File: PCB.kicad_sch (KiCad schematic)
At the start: 57 parts, among them J1 USB_C_Receptacle_USB2.0_16P, J10 Conn_01x05_Pin, J11 Conn_01x05_Pin, J12 Conn_01x03_Pin, J2 Conn_01x04_Pin, J3 Conn_01x04_Pin, J4 Conn_01x07_Pin, J5 Conn_01x02_Pin, J6 Conn_01x02_Pin, J7 Conn_01x02_Pin, J8 Conn_01x04_Pin, J9 Conn_01x07_Pin, SW1 SW_Push, SW2 SW_Push, U1 TMC2209_SILENTSTEPSTICK, U2 TMC2209_SILENTSTEPSTICK, U3 D3V3XA4B10LP, U4 AMS1117-3.3 (UMW), U5 TMC2209_SILENTSTEPSTICK, U6 ESP32-S3-WROOM-1

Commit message: Dernier DRC après modicifications
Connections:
- net GND: now also J11.1 (Pin_1), J11.2 (Pin_2), J11.3 (Pin_3), J11.4 (Pin_4)
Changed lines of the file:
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@@
 	)
 	(junction
+		(at 393.7 130.81)
+		(diameter 0)
+		(color 0 0 0 0)
+	)
+	(junction
 		(at 373.38 146.05)
 		(diameter 0)
@@
 	)
 	(junction
+		(at 386.08 130.81)
+		(diameter 0)
+		(color 0 0 0 0)
+	)
+	(junction
 		(at 290.83 176.53)
 		(diameter 0)
@@
 	)
 	(junction
+		(at 388.62 130.81)
+		(diameter 0)
+		(color 0 0 0 0)
+	)
+	(junction
 		(at 64.77 149.86)
 		(diameter 0)
@@
 	)
 	(junction
+		(at 391.16 130.81)
+		(diameter 0)
+		(color 0 0 0 0)
+	)
+	(junction
 		(at 373.38 143.51)
 		(diameter 0)
@@
 	(wire
 		(pts
+			(xy 388.62 130.81) (xy 391.16 130.81)
+		)
+		(stroke
+			(width 0)
+			(type default)
+		)
+	)
+	(wire
+		(pts
 			(xy 71.12 222.25) (xy 80.01 222.25)
 		)
@@
 	(wire
 		(pts
+			(xy 386.08 130.81) (xy 388.62 130.81)
+		)
+		(stroke
+			(width 0)
+			(type default)
+		)
+	)
+	(wire
+		(pts
 			(xy 71.12 222.25) (xy 71.12 223.52)
 		)
@@
 	(wire
 		(pts
+			(xy 393.7 130.81) (xy 396.24 130.81)
+		)
+		(stroke
+			(width 0)
+			(type default)
+		)
+	)
+	(wire
+		(pts
 			(xy 181.61 233.68) (xy 189.23 233.68)
 		)
@@
 	(wire
 		(pts
+			(xy 391.16 130.81) (xy 393.7 130.81)
+		)
+		(stroke
+			(width 0)
+			(type default)
+		)
+	)
+	(wire
+		(pts
 			(xy 74.93 58.42) (xy 80.01 58.42)
 		)
@@
 	(wire
 		(pts
-			(xy 396.24 130.81) (xy 396.24 140.97)
-		)
-		(stroke
-			(width 0)
-			(type default)
-		)
-	)
-	(wire
-		(pts
 			(xy 34.29 124.46) (xy 39.37 124.46)
 		)
@@
 	(symbol
 		(lib_id "power:GND")
-		(at 396.24 140.97 0)
+		(at 386.08 130.81 270)
 		(unit 1)
 		(exclude_from_sim no)
@@
 		(fields_autoplaced yes)
 		(property "Reference" "#PWR033"
-			(at 396.24 147.32 0)
+			(at 379.73 130.81 0)
 			(effects
 				(font
@@
 		)
 		(property "Value" "GND"
-			(at 396.24 146.05 0)
+			(at 382.27 130.8099 90)
 			(effects
 				(font
 					(size 1.27 1.27)
 				)
+				(justify right)
 			)
 		)
 		(property "Footprint" ""
-			(at 396.24 140.97 0)
+			(at 386.08 130.81 0)
 			(effects
 				(font
@@
 		)
 		(property "Datasheet" ""
-			(at 396.24 140.97 0)
+			(at 386.08 130.81 0)
 			(effects
 				(font
@@
 		)
 		(property "Description" "Power symbol creates a global label with name \"GND\" , ground"
-			(at 396.24 140.97 0)
+			(at 386.08 130.81 0)
 			(effects
 				(font

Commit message: Test DRC OK
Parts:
- C5: footprint Resistor_SMD:R_0603_1608Metric -> Capacitor_SMD:C_1206_3216Metric_Pad1.33x1.80mm_HandSolder
- R2, R3: footprint Resistor_SMD:R_01005_0402Metric -> Resistor_SMD:R_0805_2012Metric_Pad1.20x1.40mm_HandSolder
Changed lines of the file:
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@@
 			)
 		)
-		(property "Footprint" "Resistor_SMD:R_01005_0402Metric"
+		(property "Footprint" "Resistor_SMD:R_0805_2012Metric_Pad1.20x1.40mm_HandSolder"
 			(at 78.232 50.8 90)
 			(effects
@@
 			)
 		)
-		(property "Footprint" "Resistor_SMD:R_0603_1608Metric"
+		(property "Footprint" "Capacitor_SMD:C_1206_3216Metric_Pad1.33x1.80mm_HandSolder"
 			(at 122.8852 134.62 0)
 			(effects
@@
 			)
 		)
-		(property "Footprint" "Resistor_SMD:R_01005_0402Metric"
+		(property "Footprint" "Resistor_SMD:R_0805_2012Metric_Pad1.20x1.40mm_HandSolder"
 			(at 73.152 54.61 90)
 			(effects

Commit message: V2 avec test DRC OK
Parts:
- removed ADD1, J2, UART1: Conn_01x04_Pin, Connector_PinHeader_2.54mm:PinHeader_1x04_P2.54mm_Vertical, symbol Connector:Conn_01x04_Pin
- removed C6: 100uF, Capacitor_THT:CP_Radial_D10.0mm_P5.00mm, symbol Device:C
- removed J4: Conn_01x07_Pin, Connector_PinHeader_2.54mm:PinHeader_1x04_P2.54mm_Vertical, symbol Connector:Conn_01x04_Pin
- removed J9: Conn_01x07_Pin, Connector_PinHeader_2.54mm:PinHeader_1x03_P2.54mm_Vertical, symbol Connector:Conn_01x03_Pin
- removed JP3, JP4: Jumper_2_Open, Connector_PinHeader_2.54mm:PinHeader_1x02_P2.54mm_Vertical, symbol Jumper:Jumper_2_Open
- removed TOF1, TOF2, TOF3: Conn_01x05_Pin, Connector_PinHeader_2.54mm:PinHeader_1x05_P2.54mm_Vertical, symbol Connector:Conn_01x05_Pin
- removed U2: TMC2209_SILENTSTEPSTICK, TMC2209:MODULE_TMC2209_SILENTSTEPSTICK, symbol TMC2209_SILENTSTEPSTICK:TMC2209_SILENTSTEPSTICK
- added S1, S2, S3, S4, S5, S6, S7: Conn_01x07_Pin, Connector_PinHeader_2.54mm:PinHeader_1x03_P2.54mm_Vertical, symbol Connector:Conn_01x03_Pin
- added TOF1: Conn_01x04_Pin, Connector_PinHeader_2.54mm:PinHeader_1x04_P2.54mm_Vertical, symbol Connector:Conn_01x04_Pin
- C1, C10, C2, C4, C9, R4, R5: footprint Resistor_SMD:R_01005_0402Metric -> Resistor_SMD:R_0805_2012Metric_Pad1.20x1.40mm_HandSolder
- C7: footprint Resistor_SMD:R_0603_1608Metric -> Capacitor_SMD:C_1206_3216Metric_Pad1.33x1.80mm_HandSolder
- D1, D2: footprint LED_SMD:LED_0603_1608Metric -> LED_SMD:LED_0805_2012Metric_Pad1.15x1.40mm_HandSolder
- R1: footprint Resistor_SMD:R_01005_0402Metric -> Resistor_SMD:R_1206_3216Metric_Pad1.30x1.75mm_HandSolder
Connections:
- net DIR3 is gone; now on net DIR2: U5.9 (DIR), U6.8 (IO15)
- net STEP3 is gone; now on net STEP2: U5.10 (STEP), U6.19 (IO11)
- net DIR2: no longer U6.9 (IO16)
- net GND: now also S1.1 (Pin_1), S2.1 (Pin_1), S3.1 (Pin_1), S4.1 (Pin_1), S5.1 (Pin_1), S6.1 (Pin_1), S7.1 (Pin_1), TOF1.3 (Pin_3)
- net GPIO21: now also S1.3 (Pin_3)
- net GPIO35: now also S3.3 (Pin_3)
- net GPIO36: now also S4.3 (Pin_3)
- net GPIO37: now also S5.3 (Pin_3)
- net GPIO38: now also S6.3 (Pin_3)
- net GPIO47: now also S7.3 (Pin_3)
- net GPIO48: now also S2.3 (Pin_3)
- net SCL: now also TOF1.2 (Pin_2)
- net SDA: now also TOF1.1 (Pin_1)
- net STEP2: no longer U6.20 (IO12)
- net VCC_5V: now also S1.2 (Pin_2), S2.2 (Pin_2), S3.2 (Pin_2), S4.2 (Pin_2), S5.2 (Pin_2), S6.2 (Pin_2), S7.2 (Pin_2), TOF1.4 (Pin_4)
- net XSHUT1 renamed GPIO8
- net XSHUT2 renamed GPIO9
- net XSHUT3 renamed GPIO10
- new net GPIO12: U6.20 (IO12)
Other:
- note added: "2x TMC2209 Drivers to control 2x NEMA 17 with 1A/phase each +Jumper to control step"
- note added: "I2C Protocol to control 2 Devices"
- note removed: "3x TMC2209 Drivers to control 3x NEMA 17 with 1A/phase each +Jumper to control step"
- note removed: "I2C Protocol to control 4 Devices and 1 INPUT to add more"
- moved on the sheet: UART0

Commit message: debut V3
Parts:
- removed BZ1: Buzzer, Buzzer_Beeper:Buzzer_12x9.5RM7.6, symbol Device:Buzzer
- removed D2: ~, LED_SMD:LED_0805_2012Metric_Pad1.15x1.40mm_HandSolder, symbol LED:SFH482
- removed H1, H2, H3, H4: MountingHole, MountingHole:MountingHole_3.2mm_M3, symbol Mechanical:MountingHole
- removed J10, J11: Conn_01x05_Pin, Connector_PinHeader_2.54mm:PinHeader_1x05_P2.54mm_Vertical, symbol Connector:Conn_01x05_Pin
- removed J12: Conn_01x03_Pin, Connector_PinHeader_2.54mm:PinHeader_1x03_P2.54mm_Vertical, symbol Connector:Conn_01x03_Pin
- removed JP5, JP6: Jumper_2_Open, Connector_PinHeader_2.54mm:PinHeader_1x02_P2.54mm_Vertical, symbol Jumper:Jumper_2_Open
- removed JP7, JP8: Jumper_2_Open, Resistor_SMD:R_1206_3216Metric_Pad1.30x1.75mm_HandSolder, symbol Jumper:Jumper_2_Open
- removed S1, S2, S3, S4, S5, S6, S7: Conn_01x07_Pin, Connector_PinHeader_2.54mm:PinHeader_1x03_P2.54mm_Vertical, symbol Connector:Conn_01x03_Pin
- removed SCREEN1, TOF1: Conn_01x04_Pin, Connector_PinHeader_2.54mm:PinHeader_1x04_P2.54mm_Vertical, symbol Connector:Conn_01x04_Pin
- removed U3: D3V3XA4B10LP, Package_DFN_QFN:Diodes_UDFN-10_1.0x2.5mm_P0.5mm, symbol Power_Protection:D3V3XA4B10LP
- added D2: SMLVN6RGB, LED_SMD:LED_RGB_5050-6, symbol LED:SMLVN6RGB
- added F1: Fuse, Fuse:Fuse_1206_3216Metric, symbol Device:Fuse
- added H1, H2, H3, H4: MountingHole_Pad, MountingHole:MountingHole_3.2mm_M3_Pad, symbol Mechanical:MountingHole_Pad
- added J13, J4, J9: Conn_01x06_Pin, Connector_PinHeader_2.54mm:PinHeader_1x06_P2.54mm_Vertical, symbol Connector:Conn_01x06_Pin
- added JP3, JP4: Jumper_2_Open, Connector_PinHeader_2.54mm:PinHeader_1x02_P2.54mm_Vertical, symbol Jumper:Jumper_2_Open
- added R6: 10k, Resistor_SMD:R_1206_3216Metric_Pad1.30x1.75mm_HandSolder, symbol Device:R
- added R7, R8, R9: 120, Resistor_SMD:R_0805_2012Metric_Pad1.20x1.40mm_HandSolder, symbol Device:R
- added SCREEN2, TOF2, UART1: Conn_01x04_Pin, Connector_PinHeader_2.54mm:PinHeader_1x04_P2.54mm_Vertical, symbol Connector:Conn_01x04_Pin
- added U2: USBLC6-2SC6, Package_TO_SOT_SMD:SOT-23-6_Handsoldering, symbol Power_Protection:USBLC6-2SC6
- R5: value 120 -> 10k; footprint Resistor_SMD:R_0805_2012Metric_Pad1.20x1.40mm_HandSolder -> Resistor_SMD:R_1206_3216Metric_Pad1.30x1.75mm_HandSolder
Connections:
- net GPIO35 is gone; now on net STEP1: U6.28 (IO35)
- net GPIO36 is gone; now on net DIR1: U6.29 (IO36)
- net GPIO37 is gone; now on net STEP2: U6.30 (IO37)
- net GPIO38 is gone; now on net DIR2: U6.31 (IO38)
- net DIR1: no longer U6.22 (IO14)
- net DIR2: no longer U6.8 (IO15)
- net GND: now also D2.4 (GK), D2.5 (RK), D2.6 (BK), H1.1, H2.1, H3.1, H4.1, J13.1 (Pin_1), J13.2 (Pin_2), J13.3 (Pin_3), J13.4 (Pin_4), J13.5 (Pin_5), J13.6 (Pin_6), SCREEN2.4 (Pin_4), TOF2.3 (Pin_3), U2.2 (GND), UART1.1 (Pin_1); no longer R5.2
- net GPIO21: now also J4.6 (Pin_6)
- net GPIO9: now also J4.4 (Pin_4)
- net RX1: now also UART1.2 (Pin_2)
- net SCL: now also R5.2, SCREEN2.2 (Pin_2), TOF2.2 (Pin_2)
- net SDA: now also R6.2, SCREEN2.1 (Pin_1), TOF2.1 (Pin_1)
- net STEP1: no longer U6.21 (IO13)
- net STEP2: no longer U6.19 (IO11)
- net TX1: now also UART1.3 (Pin_3)
- net USB_N: now also U2.4 (I/O2); no longer J1.A7 (D-), J1.B7 (D-)
- net USB_P: now also U2.6 (I/O1); no longer J1.A6 (D+), J1.B6 (D+)
- net VCC_5V: now also R5.1, J9.1 (Pin_1), J9.2 (Pin_2), J9.3 (Pin_3), J9.4 (Pin_4), J9.5 (Pin_5), J9.6 (Pin_6), JP3.1 (A), JP4.1 (A), R6.1, SCREEN2.3 (Pin_3), TOF2.4 (Pin_4), U2.5 (VBUS), UART1.4 (Pin_4)
- net VCC_5Vin: now also F1.1; no longer J6.2 (Pin_2)
- net at U5.15 (MS1): now also JP3.2 (B)
- net GPIO16_PWM: now reaches U6.9 (IO16)
- net GPIO16_PWM: now also J4.1 (Pin_1)
- net at U5.14 (MS2): now also JP4.2 (B)
- net BUZZER renamed GPIO5
- net GPIO5: now also J4.5 (Pin_5)
- net GPIO0 renamed BOOT
- net GPIO12 renamed GPIO12_PWM
- net GPIO12_PWM: now also R8.1
- net LED renamed GPIO4
- new net: D2.3 (GA), R9.2
- new net: D2.1 (BA), R7.2
- new net: D2.2 (RA), R8.2
- new net GPIO11_PWM: R7.1, U6.19 (IO11)
- new net GPIO13_PWM: R9.1, U6.21 (IO13)
- new net GPIO14_PWM: J4.3 (Pin_3), U6.22 (IO14)
- new net GPIO15_PWM: J4.2 (Pin_2), U6.8 (IO15)
- new net USB_N_in: J1.A7 (D-), J1.B7 (D-), U2.3 (I/O2)
- new net USB_P_in: J1.A6 (D+), J1.B6 (D+), U2.1 (I/O1)
- new net VCC_5Vout: F1.2, J6.2 (Pin_2)
- no-connect marks 11 -> 9
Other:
- note added: "Analog(PWM)"
- note added: "F0 : I/O/T PINS"
- note added: "F1 : I/O/T PINS"
- note added: "Fuse"
- note added: "GPIO 43"
- note added: "GPIO 44"
- note added: "Pull-up Resistors I2C"
- note added: "Unused GPIOs F0 (I/O/T)"
- note added: "Unused GPIOs F1 (I/O/T)"
- note added: "VCC_5Vin -> Fuse -> VCC_5out -> BAU -> VCC_5V"
- note added: "}"
- note removed: "Add more 3.3V and 5V and GND pins to plug new modules"
- note removed: "Builtin LED"
- note removed: "Buzzer"
- note removed: "Can be used in input/output"
- note removed: "M1 = Phase M2 = Phase"
- note removed: "More 3V/5V & GND"
- note removed: "Normal Buzzer to make sound"
- note removed: "Pull-up Resistors"
- note removed: "Unused GPIOs"
- note removed: "VCC_5Vin -> BAU -> VCC_5V"
- moved on the sheet: C1, C10, C2, C3, C5, C7, C8, C9, D1, J1, J3, J5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

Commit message: fin du routage
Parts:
- removed TOF2: Conn_01x04_Pin, Connector_PinHeader_2.54mm:PinHeader_1x04_P2.54mm_Vertical, symbol Connector:Conn_01x04_Pin
- added J2: Conn_01x06_Socket, Connector_PinSocket_2.54mm:PinSocket_1x06_P2.54mm_Vertical, symbol Connector:Conn_01x06_Socket
- C1, C10, C2, C9: footprint Resistor_SMD:R_0805_2012Metric_Pad1.20x1.40mm_HandSolder -> Capacitor_SMD:C_0805_2012Metric_Pad1.18x1.45mm_HandSolder
- SCREEN2: footprint Connector_PinHeader_2.54mm:PinHeader_1x04_P2.54mm_Vertical -> Connector_PinSocket_2.54mm:PinSocket_1x04_P2.54mm_Vertical
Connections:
- net 3V3: now also R5.1, R6.1
- net GND: now also J2.3 (Pin_3)
- net SCL: now also J2.2 (Pin_2)
- net SDA: now also J2.1 (Pin_1)
- net USB_N: now also U2.6 (I/O1); no longer U2.4 (I/O2)
- net USB_P: now also U2.4 (I/O2); no longer U2.6 (I/O1)
- net VCC_5V: now also J2.4 (Pin_4); no longer R5.1, R6.1
- net RX0 renamed UART0-
- net RX1 renamed UART1-
- net TX0 renamed UART0+
- net TX1 renamed UART1+
- net USB_N_in renamed in_USB_N
- net in_USB_N: now also U2.1 (I/O1); no longer U2.3 (I/O2)
- net USB_P_in renamed in_USB_P
- net in_USB_P: now also U2.3 (I/O2); no longer U2.1 (I/O1)
- no-connect marks 9 -> 11
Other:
- note added: "PPTC Fuse 3.5A"
- note added: "RX"
- note added: "TX"

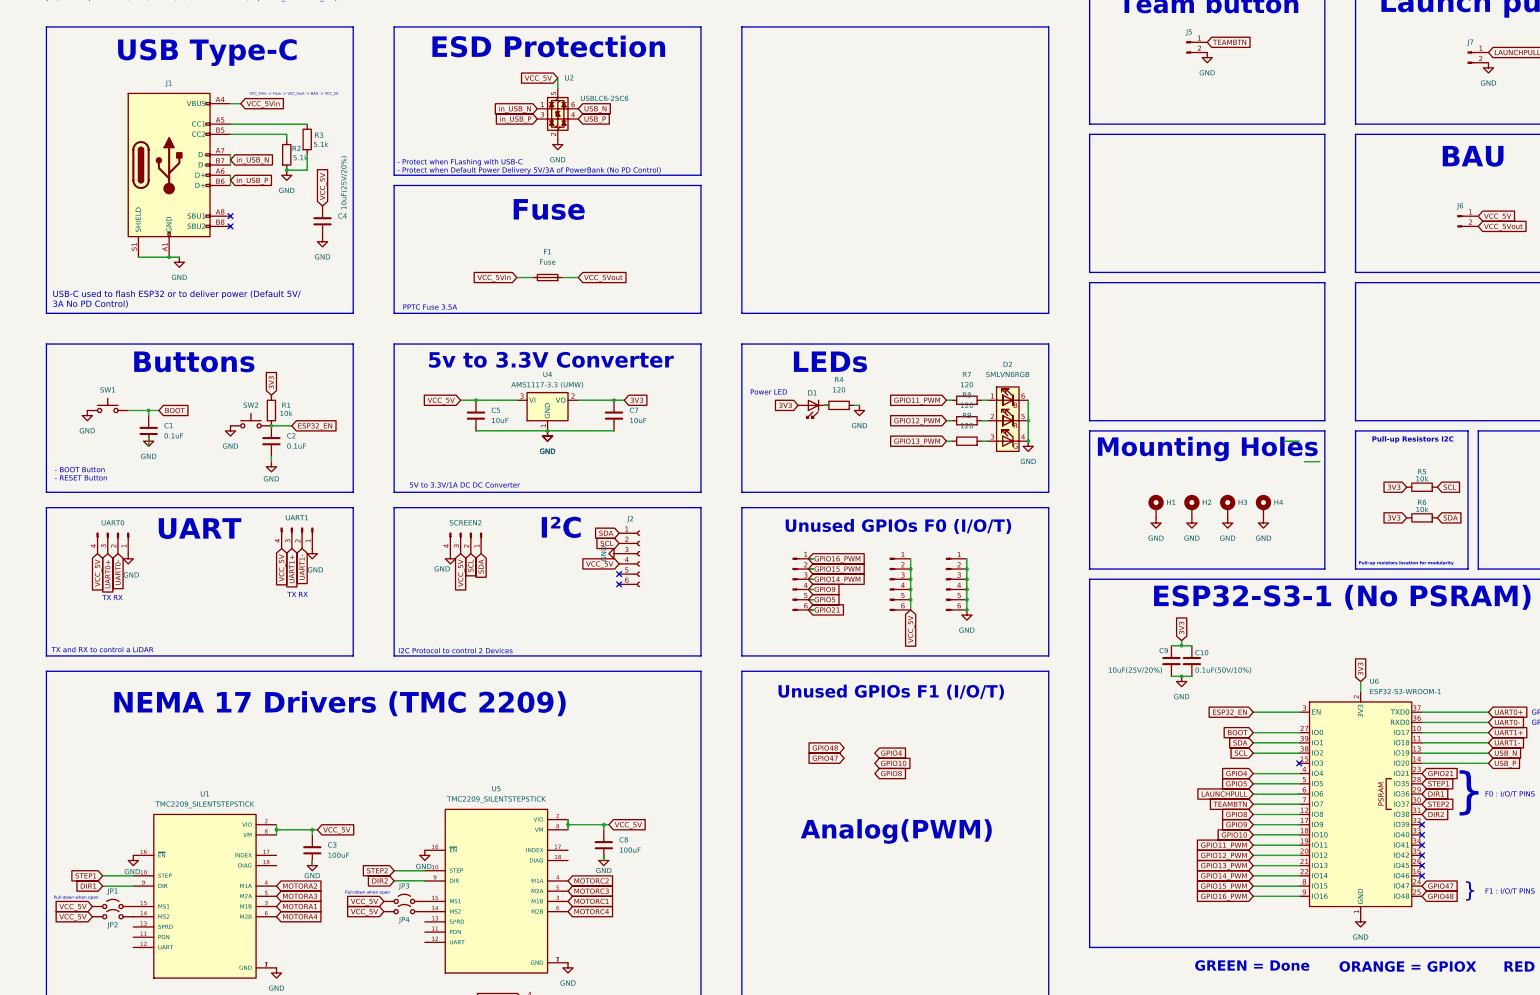
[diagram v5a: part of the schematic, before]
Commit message: ajout largeur piste + fix erreurs (DRC NOK)
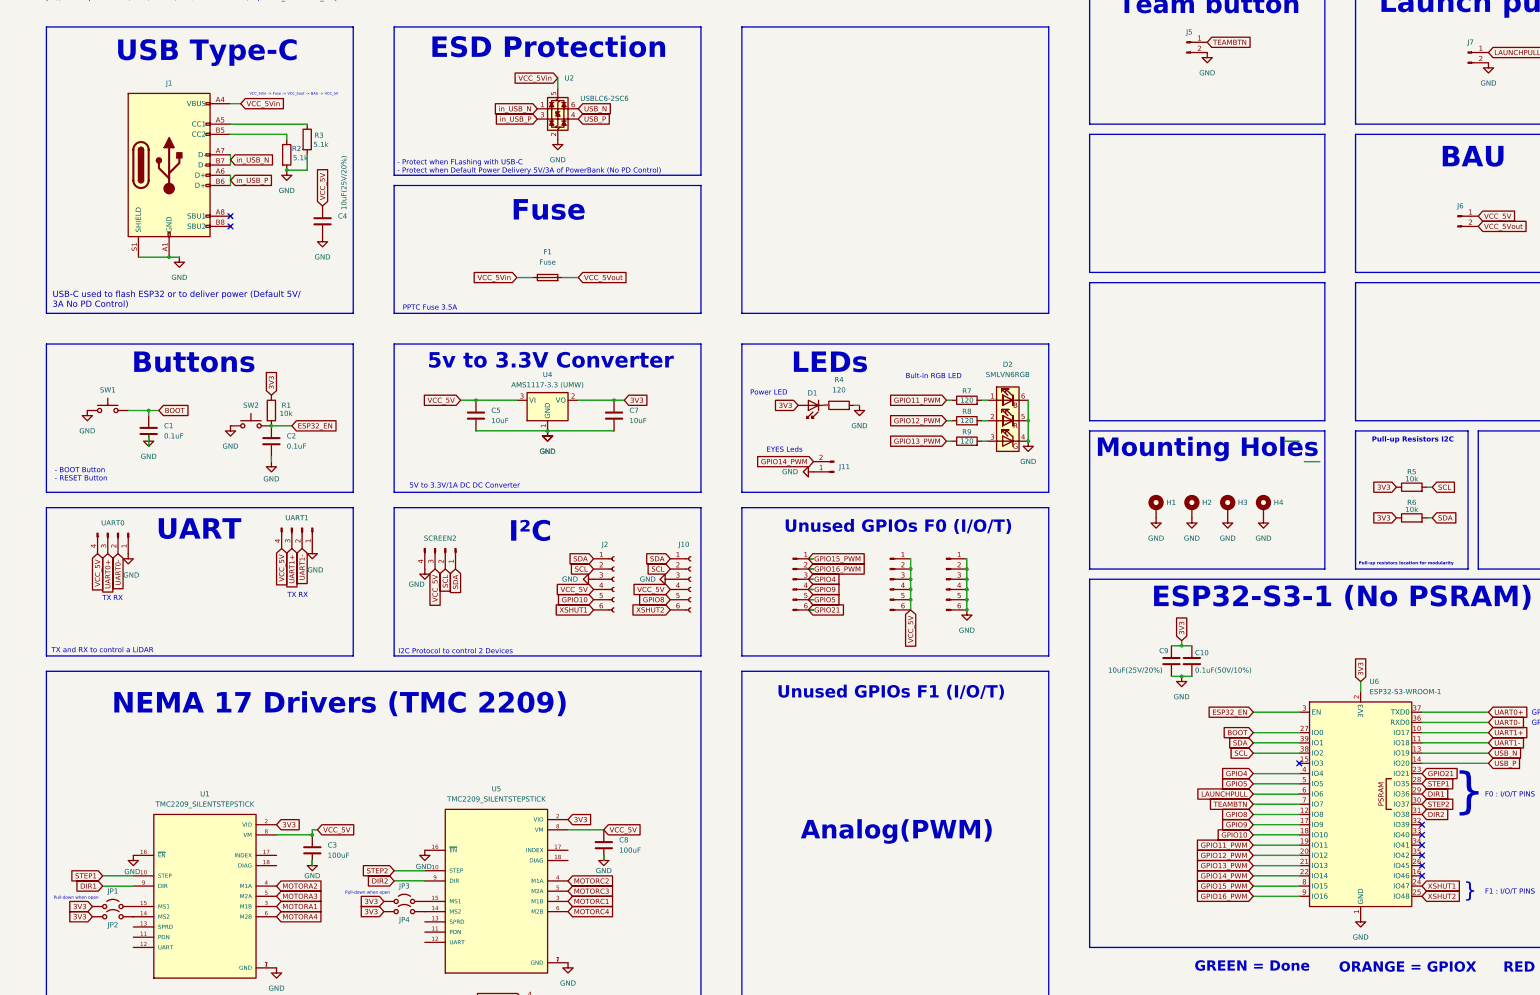
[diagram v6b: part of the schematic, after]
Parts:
- added J10: Conn_01x06_Socket, Connector_PinSocket_2.54mm:PinSocket_1x06_P2.54mm_Vertical, symbol Connector:Conn_01x06_Socket
- added J11: Conn_01x02_Pin, Connector_PinHeader_2.54mm:PinHeader_1x02_P2.54mm_Vertical, symbol Connector:Conn_01x02_Pin
- C3, C8: footprint Capacitor_THT:CP_Radial_D10.0mm_P5.00mm -> Capacitor_SMD:CP_Elec_4x5.7
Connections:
- net GPIO47 is gone; now on net XSHUT1: U6.24 (IO47)
- net 3V3: now also JP1.1 (A), JP2.1 (A), JP3.1 (A), JP4.1 (A), U1.2 (VIO), U5.2 (VIO)
- net GND: now also J10.3 (Pin_3), J11.1 (Pin_1)
- net GPIO10: now also J2.5 (Pin_5)
- net GPIO14_PWM: now also J11.2 (Pin_2); no longer J4.3 (Pin_3)
- net GPIO15_PWM: now also J4.1 (Pin_1); no longer J4.2 (Pin_2)
- net GPIO16_PWM: now also J4.2 (Pin_2); no longer J4.1 (Pin_1)
- net GPIO4: now also J4.3 (Pin_3)
- net GPIO8: now also J10.5 (Pin_5)
- net SCL: now also J10.2 (Pin_2)
- net SDA: now also J10.1 (Pin_1)
- net VCC_5V: now also J10.4 (Pin_4); no longer JP1.1 (A), JP2.1 (A), JP3.1 (A), JP4.1 (A), U1.2 (VIO), U2.5 (VBUS), U5.2 (VIO)
- net VCC_5Vin: now also U2.5 (VBUS)
- net XSHUT1: now reaches J2.6 (Pin_6)
- net GPIO48 renamed XSHUT2
- net XSHUT2: now also J10.6 (Pin_6)
- no-connect marks 11 -> 9
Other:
- note added: "Bult-in RGB LED"
- note added: "EYES Leds"
- moved on the sheet: J2, R5, R6, SCREEN2

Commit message: fin routage + faire Trou Screen gnd
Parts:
- added JP5: SolderJumper_3_Open, Jumper:SolderJumper-3_P1.3mm_Open_Pad1.0x1.5mm, symbol Jumper:SolderJumper_3_Open
- J13, J4, J9: value Conn_01x06_Pin -> Conn_01x05_Pin; footprint Connector_PinHeader_2.54mm:PinHeader_1x06_P2.54mm_Vertical -> Connector_PinHeader_2.54mm:PinHeader_1x05_P2.54mm_Vertical; symbol Connector:Conn_01x06_Pin -> Connector:Conn_01x05_Pin
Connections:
- net 3V3: now also JP5.3 (B)
- net GND: no longer J13.6 (Pin_6), U1.16 (~{EN}), U5.16 (~{EN})
- net GPIO14_PWM: now also JP5.1 (A); no longer J11.2 (Pin_2)
- net GPIO21: now also U1.16 (~{EN}), U5.16 (~{EN}); no longer J4.6 (Pin_6)
- net VCC_5V: no longer J9.6 (Pin_6)
- new net: J11.2 (Pin_2), JP5.2 (C)
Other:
- note added: "ESP32-S3-1U (No PSRAM)"
- note removed: "ESP32-S3-1 (No PSRAM)"
- moved on the sheet: H1, H2, H3, H4

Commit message: V3 Corrigée (ToF)
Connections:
- net GND: now also J10.2 (Pin_2), J2.2 (Pin_2); no longer J10.3 (Pin_3), J2.3 (Pin_3)
- net SCL: now also J10.3 (Pin_3), J2.3 (Pin_3); no longer J10.2 (Pin_2), J2.2 (Pin_2)
- net SDA: now also J10.4 (Pin_4), J2.4 (Pin_4); no longer J10.1 (Pin_1), J2.1 (Pin_1)
- net VCC_5V: now also J10.1 (Pin_1), J2.1 (Pin_1); no longer J10.4 (Pin_4), J2.4 (Pin_4)
